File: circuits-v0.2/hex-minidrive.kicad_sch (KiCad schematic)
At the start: 53 parts

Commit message: Tentatively finish new schematic.
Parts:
- removed C1, C2: 0.1uF, symbol Device:C
- removed C10, C11, C12: 1uF, components_footprints:C0603, symbol components_schematics:CL10A105KB8NNNC
- removed C13, C22: 100nF, components_footprints:C0603, symbol components_schematics:CC0603KRX7R9BB104
- removed C14, C15, C16, C17, C23: 10uF, components_footprints:C1206, symbol components_schematics:CL31A106KBHNNNE
- removed C3: 10uF, symbol Device:C
- removed C4, C5: 22uF, symbol Device:C
- removed C6: 75pF, symbol Device:C
- removed C7, C8: 1uF, symbol Device:C
- removed C9: 10nF, symbol Device:C
- removed L2: 300mΩ, components_footprints:L0805, symbol components_schematics:GZ2012D601TF
- removed L2: 10uH, components_footprints:L0805, symbol components_schematics:SDFL2012S100KTF
- removed LED1: ~, components_footprints:LED-ARRAY-SMD_4P-L1.6-W1.5-BR_XL-1615RGBC-RF, symbol components_schematics:XL-1615RGBC-RF
- removed R12, R13, R14: 1.5kΩ, components_footprints:R0603, symbol components_schematics:0603WAF1501T5E
- removed R5: 49.9 Ohm, symbol Device:R
- removed R6: 100kOhm, symbol Device:R
- removed R7: 13.3kOhm, symbol Device:R
- removed R8, R9: 5100 Ohm, symbol Device:R
- removed U2: ~, Library:QFN-16_L3.0-W3.0-P0.50-TL-EP1.7, symbol Library:EG3033_C20416138 3-half-bridge driver
- removed U6: ~, components_footprints:AMS1117-3.3 SOT-223-3_L6.5-W3.4-P2.30-LS7.0-BR, symbol components_schematics:AMS1117-3.3
- removed U7: ~, components_footprints:INA4181A1 TSSOP-20_L6.5-W4.4-P0.65-LS6.4-BL, symbol components_schematics:INA4181A1IPWR
- removed USB1: ~, Library:USB-C-SMD_TYPE-C16PIN, symbol Library:TYPE-C16PIN
- added C1, C13, C18, C19, C2, C22, C24, C25, C26, C27, C29: 100nF, ProLib_pcs_2025-10-06 (5):C0603, symbol Library:CC0603KRX7R9BB104 Capacitor 100nF
- added C10, C11, C14, C15, C16, C17, C28, C3: 10uF, Library:C1206, symbol Library:CL31A106KBHNNNE Capacitor 10uF
- added C12, C23, C7, C8: 1uF, Library:C0603, symbol Library:CL10A105KB8NNNC Capacitor 1uF
- added C20, C21: 15pF, Library:C0603, symbol Library:CL10C150JB8NNNC Capacitor 15pF
- added C30, C31, C32, C33, C35: 1nF, Library:C0603, symbol Library:CL10B102KB8NNNC Capacitor 1nF
- added C34, C9: 10nF, Library:C0603, symbol Library:0603B103K500NT Capacitor 10nF
- added C4, C5: 22uF, Library:C0805, symbol Library:CL21A226MAQNNNE Capacitor 22uF
- added C6: 100pF, Library:C0603, symbol Library:CL10C101JB8NNNC Capacitor 100pF
- added L2: 10uH, Library:L0805, symbol Library:SDFL2012S100KTF Inductor
- added L3: 300mΩ, Library:L0805, symbol Library:GZ2012D601TF Ferrite bead
- added LED1: ~, Library:LED-ARRAY-SMD_4P-L1.6-W1.5-BR_XL-1615RGBC-RF, symbol Library:XL-1615RGBC-RF RGB LED
- added R10: 49.9Ω, Library:R0603, symbol Library:0603WAF499JT5E Resistor 49.9Ω
- added R11, R12, R13: 1.5kΩ, Library:R0603, symbol Library:0603WAF1501T5E Resistor 1.5kΩ
- added R14, R15, R20, R22, R23, R24, R26, R27, R29, R9: 10Ω, Library:R0603, symbol Library:0603WAF100JT5E Resistor 10Ω
- added R16, R18, R19: 10kΩ, Library:R0603, symbol Library:0603WAF1002T5E Resistor 10kΩ
- added R17, R21, R28, R31, R32, R5: 100kΩ, Library:R0603, symbol Library:0603WAF1003T5E Resistor 100kΩ
- added R25, R30, R33, R34, R7, R8: 5.1kΩ, Library:R0603, symbol Library:0603WAF5101T5E Resistor 5.1kΩ
- added R6: 13kΩ, Library:R0603, symbol Library:0603WAF1302T5E Resistor 13kΩ
- added U6: ~, Library:QFN-16_L3.0-W3.0-P0.50-TL-EP1.7, symbol Library:EG3033_C20416138 3-half-bridge driver
- added U8: ~, Library:TSSOP-20_L6.5-W4.4-P0.65-LS6.4-BL, symbol Library:INA4181A1IPWR Current amplifier
- added USB1: ~, Library:USB-C-SMD_TYPE-C16PIN, symbol Library:TYPE-C16PIN USB connector
- added X1: 16MHz, Library:OSC-SMD_4P-L3.2-W2.5-BL, symbol Library:X322516MLB4SI Crystal oscillator 16MHz
- D1: LCSC Part # (none) -> C8598
- D2: LCSC Part # (none) -> C32677
- L1: LCSC Part # (none) -> C602033
- Q1, Q3, Q5, Q7: LCSC Part # (none) -> C315567
- Q2, Q4, Q6, Q8: LCSC Part # (none) -> C541711
- R1, R2, R3, R4: LCSC Part # (none) -> C7467248
- U1: LCSC Part # (none) -> C20416138
- U3: LCSC Part # (none) -> C2969807
- U4: LCSC Part # (none) -> C191884
- U5: LCSC Part # (none) -> C5270278
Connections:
- net Buck-5V is gone; now on net 5V: L1.2
- net 3V3: now also U5.1 (VBAT), U5.16 (VDD), U5.32 (VDD), U5.48 (VDD), U5.64 (VDD), C18.2, C24.2, C25.2, C26.2, C27.2, C8.2, L2.1, LED1.2 (COM+), U8.5 (VS)
- net 5V: now also D1.1 (-), C4.2, C5.2, C7.2, R10.2
- net Buck-FB: now also C6.1, R5.1, R6.2
- net GND: now also R1.2 (Shunt-2), R2.2 (Shunt-2), R3.2 (Shunt-2), R4.2 (Shunt-2), U1.14 (GND), U1.15 (HIN3), U1.2 (LIN3), U5.15 (VSS), U5.27 (VSSA), U5.31 (VSS), U5.47 (VSS), U5.63 (VSS), C10.1, C11.1, C12.1, C13.1, C14.1, C15.1, C16.1, C17.1, C18.1, C19.1, C2.1, C20.1, C21.1, C22.1, C23.1, C24.1, C25.1, C26.1, C27.1, C28.1, C29.1, C3.1, C30.1, C31.1, C32.1, C33.1, C34.1, C35.1, C4.1, C5.1, C7.1, C8.1, C9.1, R16.1, R18.1, R25.1, R30.1, R33.1, R34.1, R6.1, R7.1, R8.1, U6.14 (GND), U6.15 (HIN3), U6.2 (LIN3), U8.16 (GND), USB1.A1B12 (GND), USB1.B1A12 (GND), X1.2 (GND), X1.4 (GND)
- net USB_D_N: now also U5.45 (PA11), USB1.A7 (DN1), USB1.B7 (DN2)
- net USB_D_P: now also U5.46 (PA12), USB1.A6 (DP1), USB1.B6 (DP2)
- net VCC: now also Q2.1 (S), Q4.1 (S), Q6.1 (S), Q8.1 (S), U1.7 (VCC2), C10.2, C11.2, C14.2, C15.2, C16.2, C17.2, C19.2, C2.2, C28.2, C29.2, C3.2, R15.1, R17.2, R24.1, U6.7 (VCC2)
- net at Q8.2 (G): now also R29.1
- net M4: now reaches Q8.3 (D)
- net M4: now also Q7.3 (D), R32.2
- net at Q7.1 (S): now also R4.1 (Shunt-1)
- net at Q7.2 (G): now also R27.2
- net at Q1.1 (S): now also R1.1 (Shunt-1)
- net at Q1.2 (G): now also R9.2
- net M1: now reaches Q1.3 (D)
- net M1: now also Q2.3 (D), R21.2
- net at R2.1 (Shunt-1): now also Q3.1 (S)
- net +Probe-2: now reaches R2.3 (Probe-1)
- net +Probe-2: now also U8.6 (IN+2)
- net -Probe-2: now reaches R2.4 (Probe-2)
- net -Probe-2: now also U8.7 (IN±2)
- net TIM1_CH1: now reaches U1.1 (HIN1)
- net TIM1_CH1: now also U5.8 (PC0)
- net P-Gate-2: now reaches U1.10 (HO2)
- net P-Gate-2: now also R22.2
- net N-Gate-2: now reaches U1.11 (LO2)
- net N-Gate-2: now also R20.1
- net TIM1_CH2: now reaches U1.16 (HIN2)
- net TIM1_CH2: now also U5.43 (PA9)
- net TIM1_CH2N: now reaches U1.3 (LIN2)
- net TIM1_CH2N: now also U5.36 (PB14)
- net TIM1_CH1N: now reaches U1.4 (LIN1)
- net TIM1_CH1N: now also U5.2 (PC13)
- net at U1.6 (VCC1): now also R15.2
- net P-Gate-1: now reaches U1.8 (HO1)
- net P-Gate-1: now also R14.2
- net N-Gate-1: now reaches U1.9 (LO1)
- net N-Gate-1: now also R9.1
- net at Q6.2 (G): now also R26.1
- net M3: now reaches Q6.3 (D)
- net M3: now also Q5.3 (D), R31.2
- net +Probe-1: now reaches R1.3 (Probe-1)
- net +Probe-1: now also U8.4 (IN+1)
- net -Probe-1: now reaches R1.4 (Probe-2)
- net -Probe-1: now also U8.3 (IN±1)
- net at U3.4 (BYP): now also C9.2
- net at Q3.2 (G): now also R20.2
- net M2: now reaches Q3.3 (D)
- net M2: now also Q4.3 (D), R28.2
- net at L1.1, U4.2 (SW): now also C1.2
- net at D1.2 (+): now also L3.2
- net at Q5.1 (S): now also R3.1 (Shunt-1)
- net at Q5.2 (G): now also R23.2
- net at U4.6 (BOOT): now also C1.1
- net ADC1_IN8/POT_2: now reaches U5.10 (PC2)
- net TIM1_CH4: now reaches U5.11 (PC3)
- net TIM1_CH4: now also U6.16 (HIN2)
- net ADC1_IN1/M1_CURRENT: now reaches U5.12 (PA0)
- net ADC1_IN1/M1_CURRENT: now also U8.2 (OUT1)
- net ADC1_IN2/M3_CURRENT: now reaches U5.13 (PA1)
- net ADC1_IN2/M3_CURRENT: now also U8.13 (OUT3)
- net ADC1_IN3/HALF_3V3_REF: now reaches U5.14 (PA2)
- net ADC1_IN3/HALF_3V3_REF: now also U5.17 (PA3), U5.19 (PA5), U5.26 (PB2), C22.2, C23.2, R16.2, R19.1, U8.1 (REF1), U8.12 (REF3), U8.20 (REF4), U8.9 (REF2)
- net ADC2_IN17/POT_3: now reaches U5.18 (PA4)
- net ADC2_IN3/M2_CURRENT: now reaches U5.20 (PA6)
- net ADC2_IN3/M2_CURRENT: now also U8.8 (OUT2)
- net OPAMP1_VINP/M1_VOLTAGE: now reaches U5.21 (PA7)
- net OPAMP1_VINP/M1_VOLTAGE: now also C31.2, R21.1, R33.2
- net I2C2_SCL: now reaches U5.22 (PC4)
- net TIM1_CH4N: now reaches U5.23 (PC5)
- net TIM1_CH4N: now also U6.3 (LIN2)
- net OPAMP2_VINP/M2_VOLTAGE: now reaches U5.24 (PB0)
- net OPAMP2_VINP/M2_VOLTAGE: now also C32.2, R25.2, R28.1
- net TIM1_CH3N: now reaches U5.25 (PB1)
- net TIM1_CH3N: now also U6.4 (LIN1)
- net 3V3A: now reaches U5.29 (VDDA)
- net 3V3A: now also C12.2, C13.2, L2.2, R19.2
- net FREE_IO_1: now reaches U5.3 (PC14-OSC32_IN)
- net TIM2_CH3/BLUE_LED: now reaches U5.30 (PB10)
- net TIM2_CH3/BLUE_LED: now also R13.2
- net ADC2_IN14/M4_CURRENT: now reaches U5.33 (PB11)
- net ADC2_IN14/M4_CURRENT: now also U8.19 (OUT4)
- net ADC1_IN11/M4_VOLTAGE: now reaches U5.34 (PB12)
- net ADC1_IN11/M4_VOLTAGE: now also C35.2, R32.1, R34.2
- net OPAMP3_VINP/M3_VOLTAGE: now reaches U5.35 (PB13)
- net OPAMP3_VINP/M3_VOLTAGE: now also C33.2, R30.2, R31.1
- net ADC2_IN15/VOLTAGE: now reaches U5.37 (PB15)
- net ADC2_IN15/VOLTAGE: now also C30.2, R17.1, R18.2
- net TIM3_CH1/ENCODER_1: now reaches U5.38 (PC6)
- net TIM3_CH2/ENCODER_2: now reaches U5.39 (PC7)
- net FREE_IO_2: now reaches U5.4 (PC15-OSC32_OUT)
- net TIM3_CH3/ENCODER_3: now reaches U5.40 (PC8)
- net FREE_IO_3: now reaches U5.41 (PC9)
- net I2C2_SDA: now reaches U5.42 (PA8)
- net TIM1_CH3: now reaches U5.44 (PA10)
- net TIM1_CH3: now also U6.1 (HIN1)
- net SYS_JTMS-SVDIO: now reaches U5.49 (PA13)
- net at U5.5 (PF0-OSC_IN): now also C20.2, X1.1 (OSC1)
- net SYS_JTCK-SWCLK: now reaches U5.50 (PA14)
- net TIM2_CH1/RED_LED: now reaches U5.51 (PA15)
- net TIM2_CH1/RED_LED: now also R11.1
- net SPI3_SCK: now reaches U5.52 (PC10)
- net SPI3_MISO: now reaches U5.53 (PC11)
- net SPI3_MOSI: now reaches U5.54 (PC12)
- net CHIP_SELECT: now reaches U5.55 (PD2)
- net TIM2_CH2/GREEN_LED: now reaches U5.56 (PB3)
- net TIM2_CH2/GREEN_LED: now also R12.2
- net STOP_MOTOR: now reaches U5.57 (PB4)
- net TOOL_SWITCH: now reaches U5.58 (PB5)
- net USART1_TX: now reaches U5.59 (PB6)
- net at U5.6 (PF1-OSC_OUT): now also C21.2, X1.3 (OSC2)
- net USART1_RX: now reaches U5.60 (PB7)
- net I2C1_SCL: now reaches U5.61 (PB8-BOOT0)
- net I2C1_SDA: now reaches U5.62 (PB9)
- net NRST: now reaches U5.7 (PG10-NRST)
- net NRST: now also C34.2
- net ADC1_IN7/POT_1: now reaches U5.9 (PC1)
- net at Q2.2 (G): now also R14.1
- net +Probe-3: now reaches R3.3 (Probe-1)
- net +Probe-3: now also U8.15 (IN+3)
- net -Probe-3: now reaches R3.4 (Probe-2)
- net -Probe-3: now also U8.14 (IN±3)
- net at Q4.2 (G): now also R22.1
- net +Probe-4: now reaches R4.3 (Probe-1)
- net +Probe-4: now also U8.17 (IN+4)
- net -Probe-4: now reaches R4.4 (Probe-2)
- net -Probe-4: now also U8.18 (IN±4)
- new net: LED1.4 (G-), R12.1
- new net: LED1.1 (R-), R11.2
- new net: LED1.3 (B-), R13.1
- new net: C6.2, R10.1, R5.2
- new net: R7.2, USB1.A5 (CC1)
- new net: R24.2, U6.6 (VCC1)
- new net: R8.2, USB1.B5 (CC2)
- new net N-Gate-3: R23.1, U6.9 (LO1)
- new net N-Gate-4: R27.1, U6.11 (LO2)
- new net P-Gate-3: R26.2, U6.8 (HO1)
- new net P-Gate-4: R29.2, U6.10 (HO2)
- new net USB:5V: L3.1, USB1.A4B9 (VBUS), USB1.B4A9 (VBUS)
- no-connect marks 7 -> 18
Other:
- note added: "CL ~= 2 * (Cload - Cstray)"
- note added: "Driving stage"
- note added: "Ferrite bead filtering 5V USB line."
- note added: "HSE High speed external crystal oscillator for increased timing accuracy (for faster comms frequency). Internal clock has ~2% variability, good enough for motors, but not for some serial communication options."
- note added: "Microcontroller and status LED"
- note added: "TODO: need 2 connectors for i2c chiplets need connector for debug need free pin holes for direct wiring motor and 3 hall encoder need connector for high power and usart1x for bootloading and spi? 3 potentiometer connections and a solderable toggle for tool mode"
- note added: "This motor voltage is not amplified as we only need 2 voltage probes for stepper motors. However, we need the bridge voltage to verify if the mosfets were on during the driving phase."
- note added: "This small resistor is for testing purposes (so says the datasheet)."
- note added: "Use a bigger division ratio for the motor voltage because we will bias it to half VDA to measure both positive and negative EMF."
- note added: "Voltage divider 1/11, this design has max VCC of 30V."
- note added: "Voltage dividider at half point of analog voltage range for the shunt current amplifier chip. Run to a spare input so we can measure the actual reference."
- note removed: "Ferrite bead filtering from USB 5V line."
- moved on the sheet: U4

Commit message: Finish the new version schematic.
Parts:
- added FPC1, FPC2, FPC3: ~, Library:FPC-SMD_6P-P0.50_XUNPU_FPC-05F-6PH20, symbol Library:FPC-05F-6PH20 Connector 20P 0.5mm spacing FPC
- added FPC4: ~, Library:FPC-SMD_20P-P0.50_XUNPU_FPC-05F-20PH20, symbol Library:FPC-05F-20PH20 Connector 6P 0.5mm spacing FPC
- added H1, H2, H3, H4: 2.54mm 3P header, Library:HDR-TH_3P-P2.54-V-M-1, symbol Library:Header-Male-2.54_1x3 Connectors 3P 2.54mm header
- added H5: 10P 1.27mm header, Library:HDR-TH_HX-PZ1.27-1X10P-ZZ, symbol Library:HX PZ1.27-1X10P ZZ Connectors 10P 1.27mm header
- added P1: 2P 2.54mm header, Library:CONN-TH_2P-P2.50_XH-2AW, symbol Library:XH-2AW Connector 2P
- C1, C13, C2, C24, C25, C26, C27: footprint ProLib_pcs_2025-10-06 (5):C0603 -> Library:C0603
- C502: renamed from C19; footprint ProLib_pcs_2025-10-06 (5):C0603 -> Library:C0603
- C602: renamed from C29; footprint ProLib_pcs_2025-10-06 (5):C0603 -> Library:C0603
- C801: renamed from C18; footprint ProLib_pcs_2025-10-06 (5):C0603 -> Library:C0603
- C802: renamed from C22; footprint ProLib_pcs_2025-10-06 (5):C0603 -> Library:C0603
- Q1, Q3, Q5, Q7: footprint Library:DFN-8_L3.3-W3.3-P0.65-BL-2 -> Library:DFN-8_L3.0-W3.0-P0.65-BL-MOSFET
- Q2, Q4, Q6, Q8: footprint Library:DFN-8_L3.0-W3.0-P0.65-BL -> Library:DFN-8_L3.0-W3.0-P0.65-BL-MOSFET
- renumbered C31 to C101, C32 to C201, C33 to C301, C35 to C401, C17 to C501, C28 to C601, C23 to C803, R9 to R101, R14 to R102, R21 to R103, R33 to R104, R7 to R11, R8 to R12, R20 to R201, R22 to R202, R28 to R203, R25 to R204, R11 to R21, R12 to R22, R13 to R23, R23 to R301, R26 to R302, R31 to R303, R30 to R304, R27 to R401, R29 to R402, R32 to R403, R34 to R404, R15 to R501, R24 to R601, R16 to R801, R19 to R802, U5 to U1, U1 to U5
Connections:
- net I2C1_SDA is gone; now on net TIM1_CH3N: U1.62 (PB9)
- net STOP_MOTOR is gone; now on net SPI3_MISO: U1.57 (PB4)
- net USART1_RX is gone; now on net TIM4_CH2/GREEN_LED: U1.60 (PB7)
- net 3V3: now also FPC1.2, FPC2.2, FPC3.2, H1.1, H2.1, H3.1, H5.5
- net ADC1_IN7/POT_1: now also H1.2
- net ADC1_IN8/POT_2: now also H2.2
- net ADC2_IN17/POT_3: now also H3.2
- net FREE_IO_1: now also FPC2.5, FPC3.5
- net FREE_IO_2: now also FPC2.6, FPC3.6
- net GND: now also FPC1.1, FPC2.1, FPC3.1, FPC4.11, FPC4.13, FPC4.15, FPC4.17, FPC4.19, FPC4.9, H1.3, H2.3, H3.3, H4.3, H5.4, P1.1
- net I2C2_SCL: now also FPC2.4
- net I2C2_SDA: now also FPC2.3
- net M1: now also H5.6
- net M2: now also H5.7
- net M3: now also H5.8
- net M4: now also H5.9
- net NRST: now also FPC1.5, FPC4.1
- net OPAMP1_VINP/M1_VOLTAGE: now also U1.13 (PA1); no longer U1.21 (PA7)
- net OPAMP2_VINP/M2_VOLTAGE: now also U1.21 (PA7); no longer U1.24 (PB0)
- net SPI3_MISO: now also FPC4.6; no longer U1.53 (PC11)
- net SPI3_MOSI: now also FPC4.5
- net SPI3_SCK: now also U1.56 (PB3), FPC4.7; no longer U1.52 (PC10)
- net SYS_JTCK-SWCLK: now also FPC1.3
- net SYS_JTMS-SVDIO: now also FPC1.4
- net TIM1_CH3N: no longer U1.25 (PB1)
- net TIM3_CH1/ENCODER_1: now also H5.1
- net TIM3_CH2/ENCODER_2: now also H5.2
- net TIM3_CH3/ENCODER_3: now also U1.24 (PB0), H5.3; no longer U1.40 (PC8)
- net TOOL_SWITCH: now also H4.1
- net USB:5V: now also FPC1.6
- net VCC: now also FPC4.10, FPC4.12, FPC4.14, FPC4.16, FPC4.18, FPC4.20, P1.2
- net ADC1_IN2/M3_CURRENT renamed ADC1_IN12/M3_CURRENT
- net ADC1_IN12/M3_CURRENT: now also U1.25 (PB1); no longer U1.13 (PA1)
- net CHIP_SELECT renamed DIRECTION_SWITCH
- net DIRECTION_SWITCH: now also H4.2
- net FREE_IO_3 renamed I2C3_SDA
- net I2C3_SDA: now also FPC3.3
- net I2C1_SCL renamed BOOT0/STOP
- net BOOT0/STOP: now also FPC4.2
- net TIM2_CH1/RED_LED renamed SPI3_NSS
- net SPI3_NSS: now also FPC4.8; no longer R21.1
- net TIM2_CH2/GREEN_LED renamed TIM4_CH2/GREEN_LED
- net TIM4_CH2/GREEN_LED: no longer U1.56 (PB3)
- net USART1_TX renamed TIM4_CH1/RED_LED
- net TIM4_CH1/RED_LED: now also R21.1
- new net I2C3_SCL: FPC3.4, U1.40 (PC8)
- new net M-Center: H5.10
- new net USART3_RX: FPC4.3, U1.53 (PC11)
- new net USART3_TX: FPC4.4, U1.52 (PC10)
- no-connect marks 18 -> 27
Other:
- note added: "Connectors"
- note added: "Debug FPC connector"
- note added: "Hex Mini Driver This is a quad output, motor driver for stepper, brushless or 2 DC motors. The board comes provisioned with 2 I2C connectors for plug in rotation sensors AS5600 (preferably the Hex mini flex rotation sensor). Target limits are 6-30V supply range and 5A of current."
- note added: "Motor connector matches pins for some choice of motors."
- note added: "Power and control, FPC connector"
- note added: "SDA A FPC connector"
- note added: "SDA B FPC connector"
- note removed: "TODO: need 2 connectors for i2c chiplets need connector for debug need free pin holes for direct wiring motor and 3 hall encoder need connector for high power and usart1x for bootloading and spi? 3 potentiometer connections and a solderable toggle for tool mode"
- moved on the sheet: C101, C20, C201, C21, C24, C25, C26, C27, C30, C301, C34, C401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

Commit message: Update electrical design rules.
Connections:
- net LDO-Bypass-Capacitor: now reaches C9.2, U3.4 (BYP)
- net Green-LED: now reaches LED1.4 (G-), R22.1
- net Shunt-1: now reaches Q1.1 (S), R1.1 (Shunt-1)
- net Shunt-4: now reaches Q7.1 (S), R4.1 (Shunt-1)
- net Gate-2-Positive: now reaches Q4.2 (G), R202.1
- net Gate-4-Positive: now reaches Q8.2 (G), R402.1
- net Shunt-2: now reaches Q3.1 (S), R2.1 (Shunt-1)
- net Gate-4-Negative: now reaches Q7.2 (G), R401.2
- net Gate-2-Negative: now reaches Q3.2 (G), R201.2
- net Red-LED: now reaches LED1.1 (R-), R21.2
- net Blue-LED: now reaches LED1.3 (B-), R23.1
- net Buck-Probe-Point: now reaches C6.2, R10.1, R5.2
- net Gate-1-Positive: now reaches Q2.2 (G), R102.1
- net Buck-Bootstrap-Capacitor: now reaches C1.1, U4.6 (BOOT)
- net Buck-Output-SW: now reaches C1.2, L1.1, U4.2 (SW)
- net Shunt-3: now reaches Q5.1 (S), R3.1 (Shunt-1)
- net Gate-3-Negative: now reaches Q5.2 (G), R301.2
- net Gate-3-Positive: now reaches Q6.2 (G), R302.1
- net Gate-1-Negative: now reaches Q1.2 (G), R101.2

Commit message: Near final v0.2 circuit design.
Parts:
- removed C501, C601: 10uF, Library:C1206, symbol Library:CL31A106KBHNNNE Capacitor 10uF
- removed FPC1: ~, Library:FPC-SMD_6P-P0.50_XUNPU_FPC-05F-6PH20, symbol Library:FPC-05F-6PH20 Connector 20P 0.5mm spacing FPC
- removed H1, H2, H3, H4: 2.54mm 3P header, Library:HDR-TH_3P-P2.54-V-M-1, symbol Library:Header-Male-2.54_1x3 Connectors 3P 2.54mm header
- removed P1: 2P 2.54mm header, Library:CONN-TH_2P-P2.50_XH-2AW, symbol Library:XH-2AW Connector 2P
- added C17, C18: 10uF, Library:C1206, symbol Library:CL31A106KBHNNNE Capacitor 10uF
- added H2: 2P-2.54mm-header, Library:HDR-TH_2P-P2.54-V-M, symbol Library:PZ254V-11-02P Connector 2P 2.54mm spacing
- added H3: 10P 1.27mm header, Library:HDR-TH_HX-PZ1.27-1X10P-ZZ, symbol Library:HX PZ1.27-1X10P ZZ Connectors 10P 1.27mm header
- renumbered C502 to C501, C602 to C601, H5 to H1
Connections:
- net 3V3: now also H3.5
- net 5V: now also H3.4
- net ADC1_IN7/POT_1: now also H3.6
- net ADC1_IN8/POT_2: now also H3.7
- net ADC2_IN17/POT_3: now also H3.8
- net BOOT0/STOP: now also USB1.B8 (SBU2)
- net DIRECTION_SWITCH: now also H3.10
- net GND: now also U5.17 (EP), U6.17 (EP), C17.1, C18.1, H2.2, H3.1
- net NRST: now also USB1.A8 (SBU1)
- net SYS_JTCK-SWCLK: now also H3.2
- net SYS_JTMS-SVDIO: now also H3.3
- net TOOL_SWITCH: now also H3.9
- net VCC: now also C17.2, C18.2, H2.1
- net OSC1: now reaches C20.2, U1.5 (PF0-OSC_IN), X1.1 (OSC1)
- net OSC2: now reaches C21.2, U1.6 (PF1-OSC_OUT), X1.3 (OSC2)
- net Driver1-internal-LDO: now reaches R501.2, U5.6 (VCC1)
- net Driver2-internal-LDO: now reaches R601.2, U6.6 (VCC1)
- no-connect marks 27 -> 21
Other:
- note added: "Can this resistor be removed and the pin left unconnected?"
- note added: "Debug connector"
- note added: "SBU1 and SBU2 are coonected to Reset and Boot0 pins so we can flash new software over USB with the builtin bootloader, let's see if it works."
- note removed: "Debug FPC connector"
- moved on the sheet: C10, C11, C14, C15, C16, C501, C601, FPC2, FPC3, H1

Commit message: Order v0.2 circuits.
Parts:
- removed U1: ~, Library:LQFP-64_L10.0-W10.0-P0.50-LS12.0-BL, symbol Library:STM32G431RBT3TR Microcontroller
- added U1: ~, Library:LQFP-64_L10.0-W10.0-P0.50-LS12.0-BL, symbol Library:STM32G431RBT6 Microcontroller
- H1, H3: now not fitted; now left out of the parts list
- H2: now not fitted
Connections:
- net 3V3: now also U1.1 (VBAT), U1.16 (VDD), U1.32 (VDD), U1.48 (VDD), U1.64 (VDD)
- net 3V3A: now also U1.29 (VDDA)
- net ADC1_IN11/M4_VOLTAGE: now also U1.34 (PB12)
- net ADC1_IN12/M3_CURRENT: now also U1.25 (PB1)
- net ADC1_IN1/M1_CURRENT: now also U1.12 (PA0)
- net ADC1_IN3/HALF_3V3_REF: now also U1.14 (PA2), U1.17 (PA3), U1.19 (PA5), U1.26 (PB2)
- net ADC1_IN7/POT_1: now also U1.9 (PC1)
- net ADC1_IN8/POT_2: now also U1.10 (PC2)
- net ADC2_IN14/M4_CURRENT: now also U1.33 (PB11)
- net ADC2_IN15/VOLTAGE: now also U1.37 (PB15)
- net ADC2_IN17/POT_3: now also U1.18 (PA4)
- net ADC2_IN3/M2_CURRENT: now also U1.20 (PA6)
- net BOOT0/STOP: now also U1.61 (PB8-BOOT0)
- net DIRECTION_SWITCH: now also U1.55 (PD2)
- net FREE_IO_1: now also U1.3 (PC14-OSC32_IN)
- net FREE_IO_2: now also U1.4 (PC15-OSC32_OUT)
- net GND: now also U1.15 (VSS), U1.27 (VSSA), U1.31 (VSS), U1.47 (VSS), U1.63 (VSS)
- net I2C2_SCL: now also U1.22 (PC4)
- net I2C2_SDA: now also U1.42 (PA8)
- net I2C3_SCL: now also U1.40 (PC8)
- net I2C3_SDA: now also U1.41 (PC9)
- net NRST: now also U1.7 (PG10-NRST)
- net OPAMP1_VINP/M1_VOLTAGE: now also U1.13 (PA1)
- net OPAMP2_VINP/M2_VOLTAGE: now also U1.21 (PA7)
- net OPAMP3_VINP/M3_VOLTAGE: now also U1.35 (PB13)
- net OSC1: now also U1.5 (PF0-OSC_IN)
- net OSC2: now also U1.6 (PF1-OSC_OUT)
- net SPI3_MISO: now also U1.57 (PB4)
- net SPI3_MOSI: now also U1.54 (PC12)
- net SPI3_NSS: now also U1.51 (PA15)
- net SPI3_SCK: now also U1.56 (PB3)
- net SYS_JTCK-SWCLK: now also U1.50 (PA14)
- net SYS_JTMS-SVDIO: now also U1.49 (PA13)
- net TIM1_CH1: now also U1.8 (PC0)
- net TIM1_CH1N: now also U1.2 (PC13)
- net TIM1_CH2: now also U1.43 (PA9)
- net TIM1_CH2N: now also U1.36 (PB14)
- net TIM1_CH3: now also U1.44 (PA10)
- net TIM1_CH3N: now also U1.62 (PB9)
- net TIM1_CH4: now also U1.11 (PC3)
- net TIM1_CH4N: now also U1.23 (PC5)
- net TIM2_CH3/BLUE_LED: now also U1.30 (PB10)
- net TIM3_CH1/ENCODER_1: now also U1.38 (PC6)
- net TIM3_CH2/ENCODER_2: now also U1.39 (PC7)
- net TIM3_CH3/ENCODER_3: now also U1.24 (PB0)
- net TIM4_CH1/RED_LED: now also U1.59 (PB6)
- net TIM4_CH2/GREEN_LED: now also U1.60 (PB7)
- net TOOL_SWITCH: now also U1.58 (PB5)
- net USART3_RX: now also U1.53 (PC11)
- net USART3_TX: now also U1.52 (PC10)
- net USB_D_N: now also U1.45 (PA11)
- net USB_D_P: now also U1.46 (PA12)

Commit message: Update schematic information panel.
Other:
- company: (none) -> Hex Robotics Limited
- title: (none) -> Hex mini servo driver
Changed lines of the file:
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@@
 	(generator_version "9.0")
 	(paper "A2")
+	(title_block
+		(title "Hex mini servo driver")
+		(rev "version 0.2")
+		(company "Hex Robotics Limited")
+		(comment 1 "Author: Calin Mocanu")
+	)

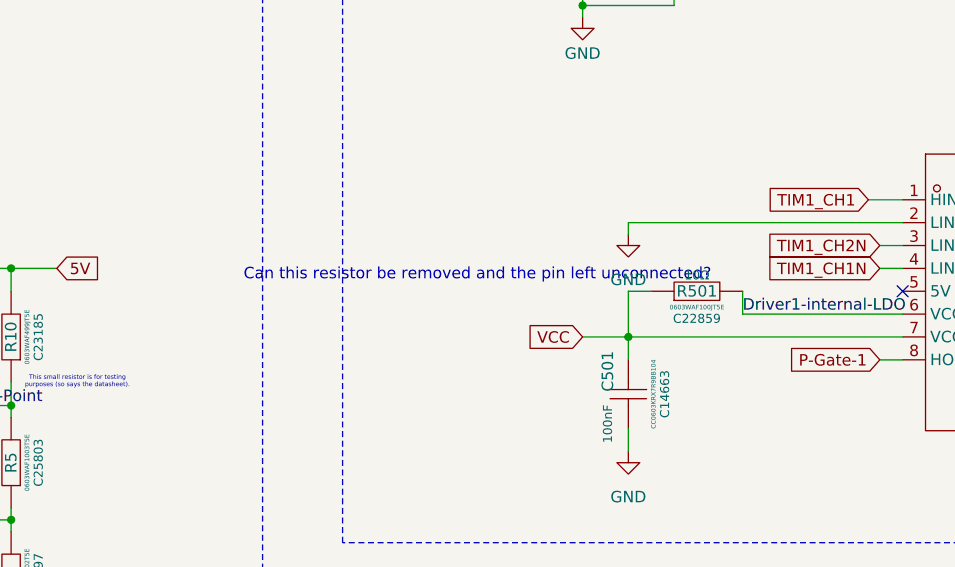
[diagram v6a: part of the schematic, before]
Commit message: Start re-wiring v0.3 motor driver, 16mm width is too tight.
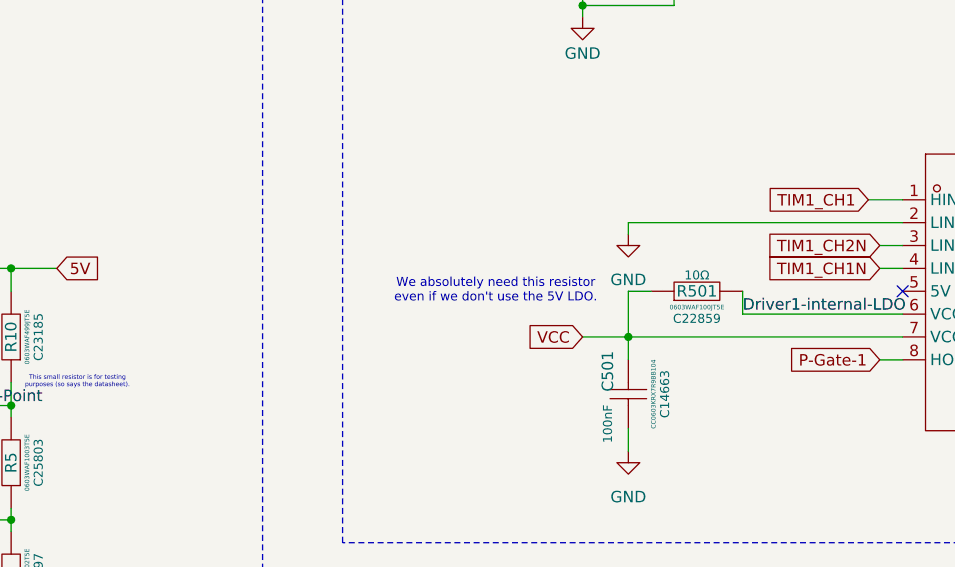
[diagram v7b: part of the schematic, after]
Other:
- note added: "We absolutely need this resistor even if we don't use the 5V LDO."
- note removed: "Can this resistor be removed and the pin left unconnected?"
